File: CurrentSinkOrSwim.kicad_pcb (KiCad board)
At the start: 2 copper layers, 41.7 x 38.9 mm, 25 parts, among them P1 CONN_01X01, P101 ext pwr, P102 pwr select, P103 Input, P2 V, P3 A, P4 Gnd, Q401 BUK9575, U201 LMV358, U301 LM2931D-R

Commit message: Routing done
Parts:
- C201, C301, C302, R401: moved to F.Cu
- P101: footprint Current:Pads-01x02 -> Pads-01x02
- P102: value pwr select -> pwr sel
- moved R201 10.4 mm to (124.0, 65.0), turned to 270 degrees
- moved C302 6.73 mm to (136.2, 64.8), turned to 270 degrees
- moved C201 6.58 mm to (121.6, 63.2), turned to 90 degrees
- moved D201 6.49 mm to (116.8, 63.0)
- moved R401 5.71 mm to (126.0, 65.0), turned to 270 degrees
- moved R301 4.29 mm to (129.4, 72.6), turned to 180 degrees
- moved R302 2.37 mm to (128.0, 65.0)
- moved R402 2.36 mm to (119.0, 63.2)
- moved U201 2.32 mm to (118.8, 68.0), turned to 270 degrees
- moved U301 1.87 mm to (132.2, 67.2)
- moved R303 1.77 mm to (128.0, 69.4)
- moved R202 1.32 mm to (123.6, 73.6), turned to 90 degrees
- moved R203 1.23 mm to (121.2, 73.6), turned to 270 degrees
- moved C301 1.14 mm to (136.2, 69.8)
- moved P101 0.90 mm to (135.0, 80.0)
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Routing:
- net (no net): track 267.2 -> 0.00 mm, vias 9 -> 0
- net /Current Control/Current_Sink+: track 0.00 -> 57.6 mm
- net GND: track 0.00 -> 33.3 mm, vias 0 -> 5
- net Net-(P3-Pad1): track 0.00 -> 29.6 mm, vias 0 -> 2
- net Net-(P2-Pad1): track 0.00 -> 28.8 mm, vias 0 -> 2
- net Net-(Q401-PadS): track 0.00 -> 26.4 mm, vias 0 -> 2
- net 2.7V: track 0.00 -> 20.1 mm
- net /Current Control/FET_Gate: track 0.00 -> 15.1 mm
- net /Power Regulation/Vin: track 0.00 -> 12.9 mm, vias 0 -> 1
- net Net-(R202-Pad2): track 0.00 -> 11.5 mm
- net Net-(R302-Pad2): track 0.00 -> 7.21 mm
- net Net-(P101-Pad2): track 0.00 -> 6.05 mm
- net Net-(R402-Pad2): track 0.00 -> 5.39 mm
- net Net-(D201-Pad2): track 0.00 -> 2.88 mm
- net Net-(R301-Pad1): track 0.00 -> 2.25 mm
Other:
- board size 41.7 x 38.9 mm -> 41 x 38 mm
- board text added: "Amp"
- board text added: "Volt"
- board text added: "int"
- board text removed: "in"

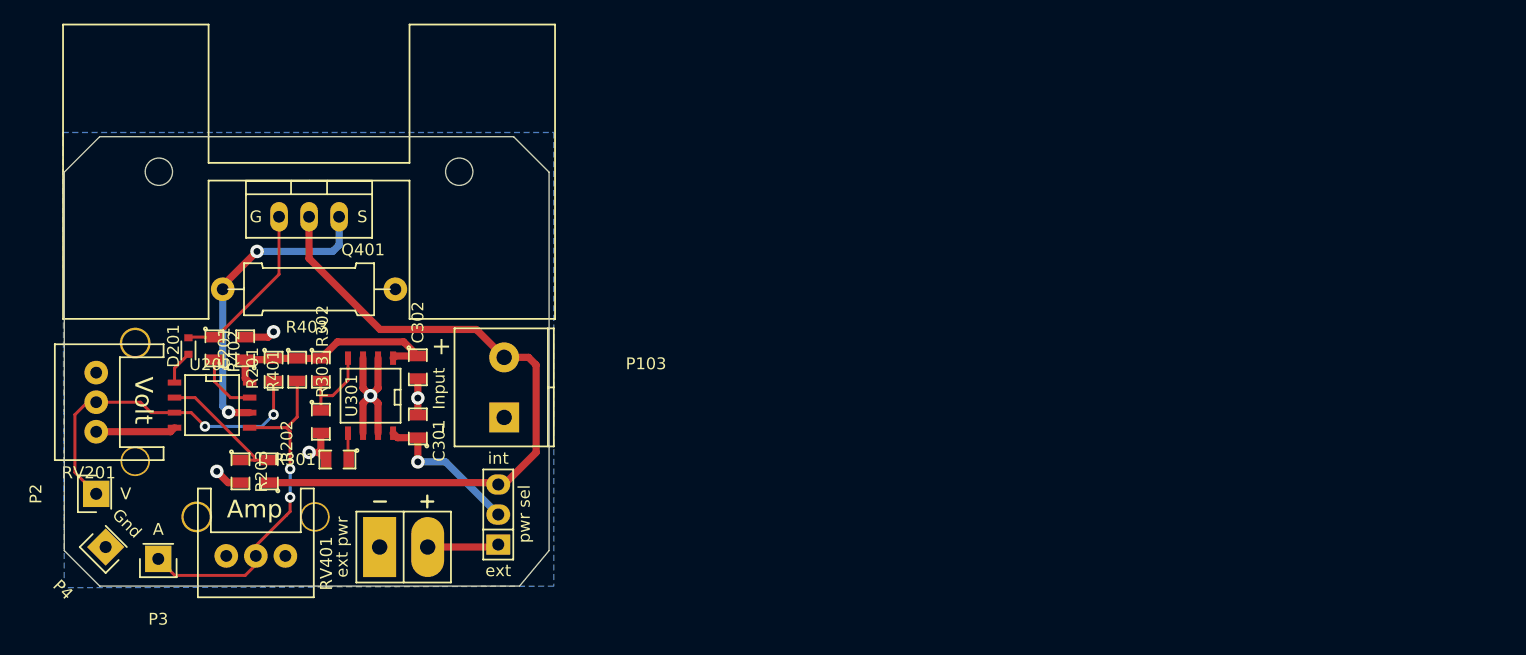
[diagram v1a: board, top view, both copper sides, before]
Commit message: Revert "Routing done"
This reverts commit 9c8e4a17aa7ae0fb22a7aeeae40aa608407b6119.

Conflicts:
	CurrentSinkOrSwim.sch
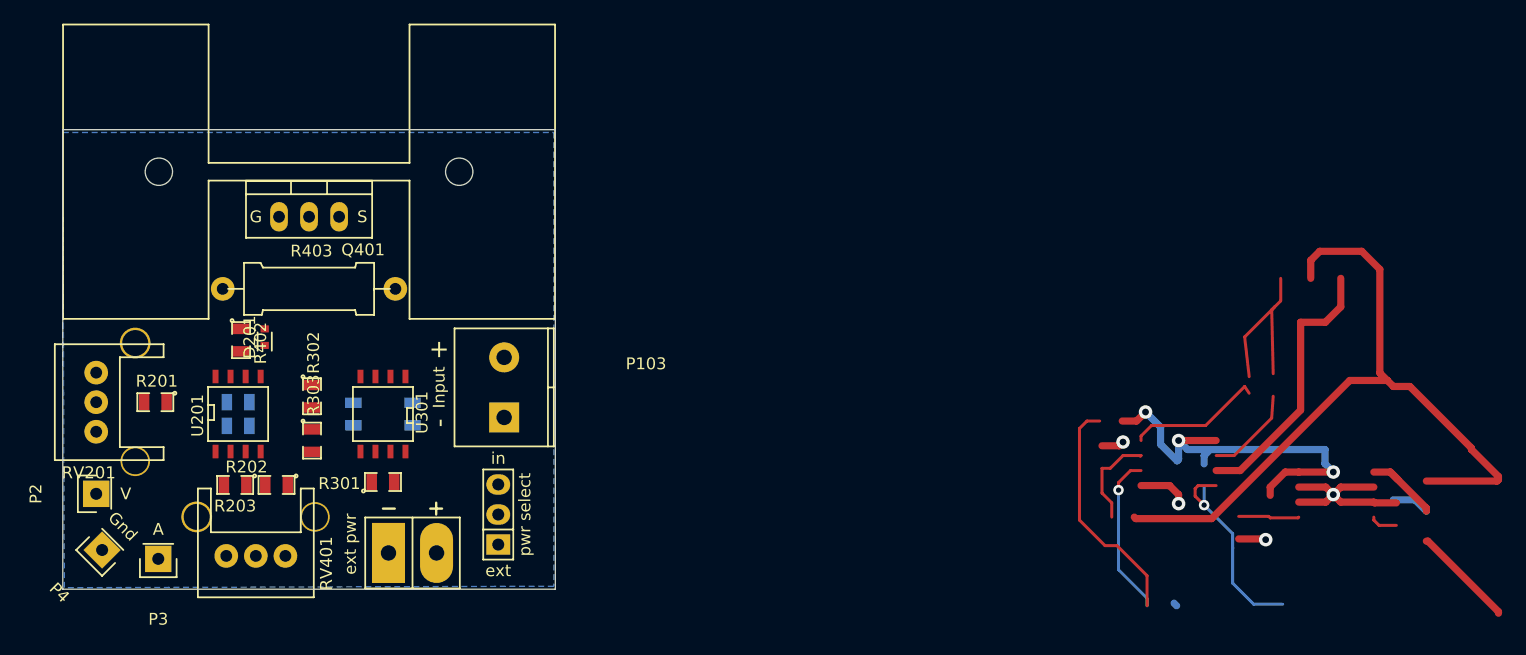
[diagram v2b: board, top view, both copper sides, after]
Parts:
- C201, C301, C302, R401: moved to B.Cu
- P101: footprint Pads-01x02 -> Current:Pads-01x02
- P102: value pwr sel -> pwr select
- moved R201 10.4 mm to (114.0, 67.8), turned to 180 degrees
- moved C302 6.73 mm to (130.8, 68.8), turned to 90 degrees
- moved C201 6.58 mm to (121.0, 69.8), turned to 0 degrees
- moved D201 6.49 mm to (123.2, 62.2)
- moved R401 5.71 mm to (121.0, 67.8), turned to 0 degrees
- moved R301 4.29 mm to (133.2, 74.5), turned to 0 degrees
- moved R302 2.37 mm to (127.2, 67.2)
- moved R402 2.36 mm to (121.2, 62.5)
- moved U201 2.32 mm to (121.0, 68.8), turned to 0 degrees
- moved U301 1.87 mm to (133.2, 68.8)
- moved R303 1.77 mm to (127.2, 71.0)
- moved R202 1.32 mm to (124.2, 74.8), turned to 180 degrees
- moved R203 1.23 mm to (120.8, 74.8), turned to 180 degrees
- moved C301 1.14 mm to (135.8, 68.8)
- moved P101 0.90 mm to (135.8, 80.5)
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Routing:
- net (no net): track 0.00 -> 267.2 mm, vias 0 -> 9
- net /Current Control/Current_Sink+: track 57.6 -> 0.00 mm
- net GND: track 33.3 -> 0.00 mm, vias 5 -> 0
- net Net-(P3-Pad1): track 29.6 -> 0.00 mm, vias 2 -> 0
- net Net-(P2-Pad1): track 28.8 -> 0.00 mm, vias 2 -> 0
- net Net-(Q401-PadS): track 26.4 -> 0.00 mm, vias 2 -> 0
- net 2.7V: track 20.1 -> 0.00 mm
- net /Current Control/FET_Gate: track 15.1 -> 0.00 mm
- net /Power Regulation/Vin: track 12.9 -> 0.00 mm, vias 1 -> 0
- net Net-(R202-Pad2): track 11.5 -> 0.00 mm
- net Net-(R302-Pad2): track 7.21 -> 0.00 mm
- net Net-(P101-Pad2): track 6.05 -> 0.00 mm
- net Net-(R402-Pad2): track 5.39 -> 0.00 mm
- net Net-(D201-Pad2): track 2.88 -> 0.00 mm
- net Net-(R301-Pad1): track 2.25 -> 0.00 mm
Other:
- board size 41 x 38 mm -> 41.7 x 38.9 mm
- board text added: "in"
- board text removed: "Amp"
- board text removed: "Volt"
- board text removed: "int"
